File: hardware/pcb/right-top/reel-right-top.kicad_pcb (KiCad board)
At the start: 2 copper layers, 143 x 86.6 mm, 24 parts, among them SW1 choc_plate, SW10 choc_plate, SW11 choc_plate, SW12 choc_plate, SW13 choc_plate, SW14 choc_plate, SW15 choc_plate, SW16 choc_plate, SW17 choc_plate, SW18 choc_plate, SW19 choc_plate, SW2 choc_plate, SW3 choc_plate, SW4 choc_plate, SW5 choc_plate, SW6 choc_plate, SW7 choc_plate, SW8 choc_plate, SW9 choc_plate

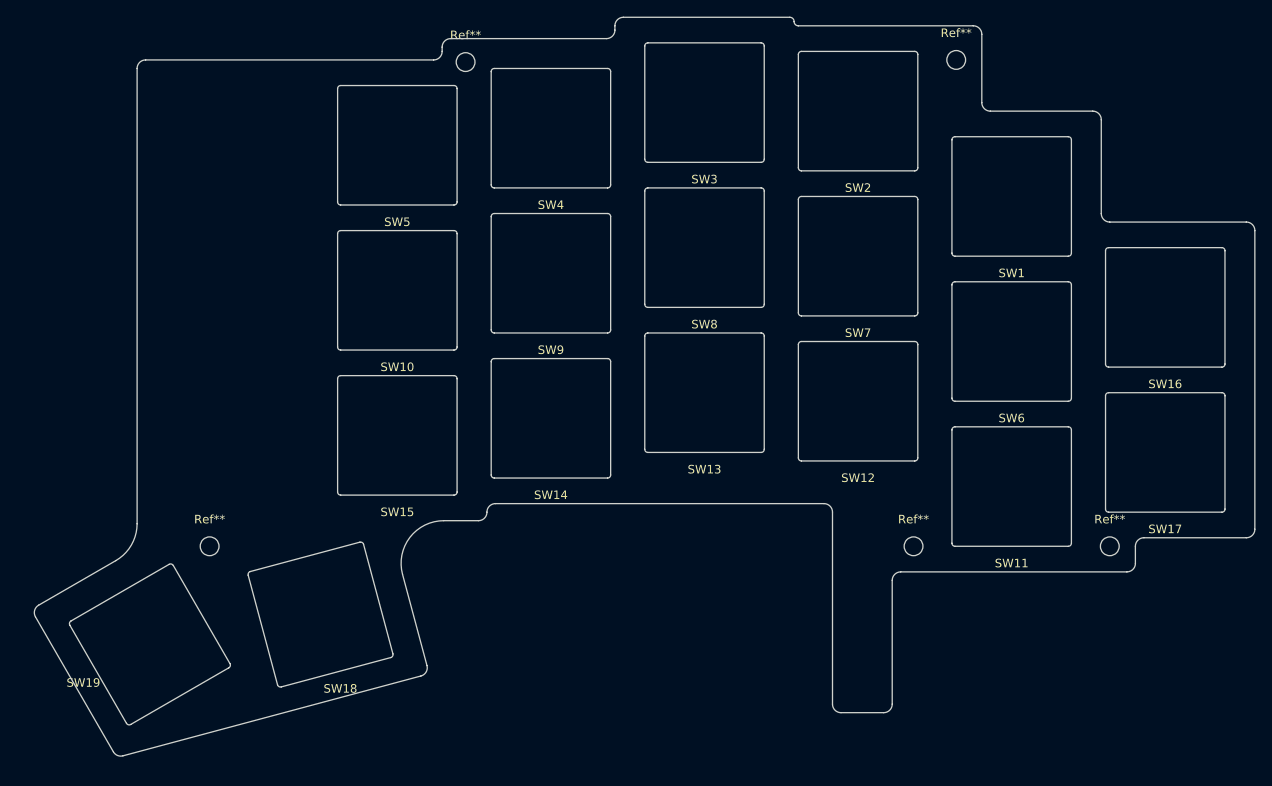
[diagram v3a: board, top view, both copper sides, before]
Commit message: Update right PCB and derived variants
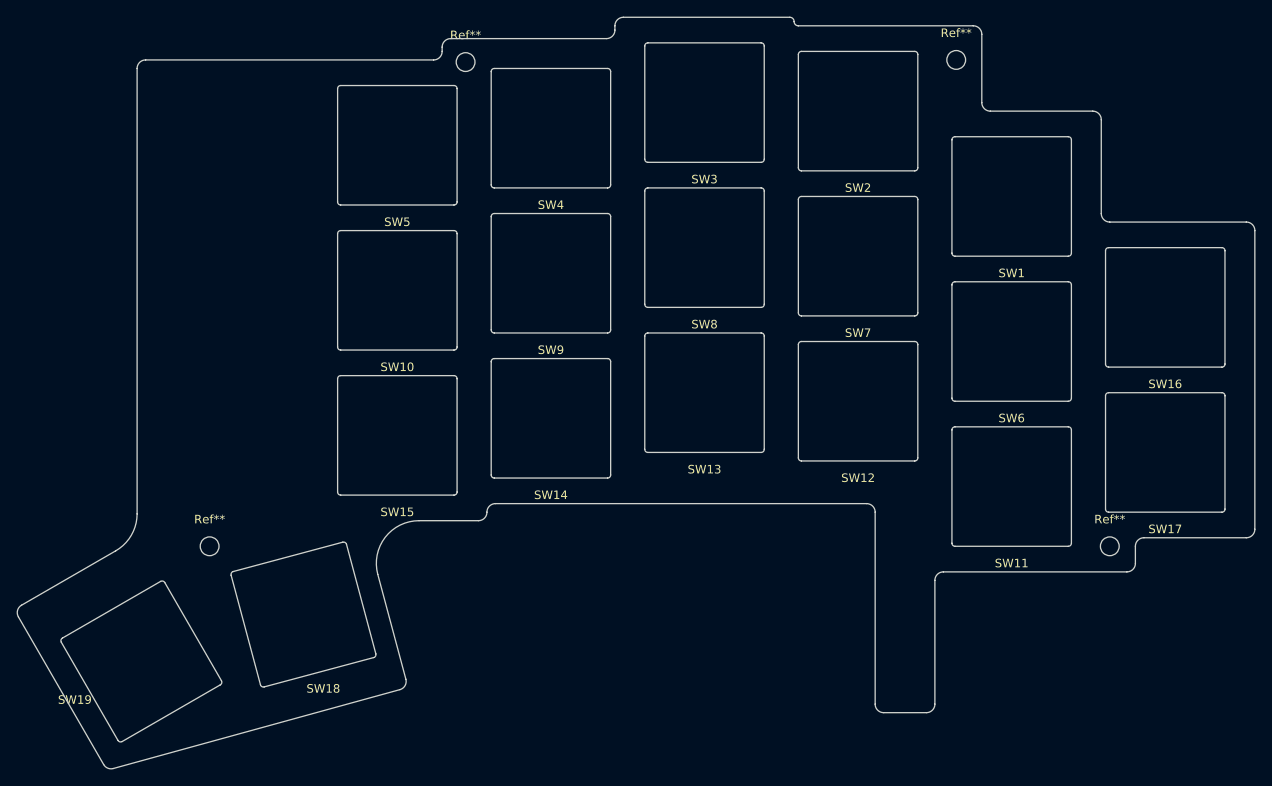
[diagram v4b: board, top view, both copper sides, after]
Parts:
- removed the Ref** at (140.5, 107.5)
- moved SW19 2.24 mm to (50.0, 121.0)
- moved SW18 2.00 mm to (69.0, 115.5)
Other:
- board size 143 x 86.6 mm -> 145 x 88.1 mm
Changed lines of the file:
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@@
 	)
 	(footprint "reel:choc_plate"
-		(generator_version "9.0")
 		(layer "F.Cu")
 		(at 116 72.5 180)
@@
 		)
 	)
-	(footprint "MountingHole:MountingHole_2.2mm_M2"
-		(layer "F.Cu")
-		(at 140.5 107.5)
-		(descr "Mounting Hole 2.2mm, M2, no annular, generated by kicad-footprint-generator mountinghole.py")
-		(tags "mountinghole M2")
-		(property "Reference" "Ref**"
-			(at 0 -3.15 0)
-			(layer "F.SilkS")
-			(effects
-				(font
-					(size 1 1)
-					(thickness 0.15)
-				)
-			)
-		)
-		(property "Value" "MountingHole_2.2mm_M2"
-			(at 0 3.15 0)
-			(layer "F.Fab")
-			(effects
-				(font
-					(size 1 1)
-					(thickness 0.15)
-				)
-			)
-		)
-		(property "KiLib_Generator" "mounting_hardware/mounting_hole"
-			(at 0 0 0)
-			(layer "F.SilkS")
-			(hide yes)
-			(effects
-				(font
-					(size 1 1)
-					(thickness 0.15)
-				)
-			)
-		)
-		(attr exclude_from_pos_files exclude_from_bom)
-		(duplicate_pad_numbers_are_jumpers no)
-		(fp_circle
-			(center 0 0)
-			(end 2.2 0)
-			(stroke
-				(width 0.15)
-				(type solid)
-			)
-			(fill no)
-			(layer "Cmts.User")
-		)
-		(fp_circle
-			(center 0 0)
-			(end 2.45 0)
-			(stroke
-				(width 0.05)
-				(type solid)
-			)
-			(fill no)
-			(layer "F.CrtYd")
-		)
-		(fp_text user "${REFERENCE}"
-			(at 0 0 0)
-			(layer "F.Fab")
-			(effects
-				(font
-					(size 1 1)
-					(thickness 0.15)
-				)
-			)
-		)
-		(pad "" np_thru_hole circle
-			(at 0 0)
-			(size 2.2 2.2)
-			(drill 2.2)
-			(layers "*.Cu" "*.Mask")
-		)
-		(embedded_fonts no)
-	)
 	(footprint "reel:choc_plate"
-		(generator_version "9.0")
 		(layer "F.Cu")
 		(at 152 100.5 180)
@@
 	)
 	(footprint "reel:choc_plate"
-		(generator_version "9.0")
 		(layer "F.Cu")
 		(at 134 90.5 180)
@@
 	)
 	(footprint "reel:choc_plate"
-		(generator_version "9.0")
 		(layer "F.Cu")
 		(at 170 96.5 180)
@@
 	)
 	(footprint "reel:choc_plate"
-		(generator_version "9.0")
 		(layer "F.Cu")
 		(at 80 60.5 180)
@@
 	)
 	(footprint "reel:choc_plate"
-		(generator_version "9.0")
 		(layer "F.Cu")
 		(at 152 66.5 180)
@@
 	)
 	(footprint "reel:choc_plate"
-		(generator_version "9.0")
 		(layer "F.Cu")
 		(at 98 75.5 180)
@@
 	)
 	(footprint "reel:choc_plate"
-		(generator_version "9.0")
 		(layer "F.Cu")
 		(at 134 56.5 180)
@@
 	)
 	(footprint "reel:choc_plate"
-		(generator_version "9.0")
 		(layer "F.Cu")
 		(at 170 79.5 180)
@@
 	)
 	(footprint "reel:choc_plate"
-		(generator_version "9.0")
 		(layer "F.Cu")
 		(at 152 83.5 180)
@@
 	)
 	(footprint "reel:choc_plate"
-		(generator_version "9.0")
 		(layer "F.Cu")
 		(at 116 55.5 180)
@@
 	)
 	(footprint "reel:choc_plate"
-		(generator_version "9.0")
 		(layer "F.Cu")
 		(at 98 92.5 180)
@@
 	)
 	(footprint "reel:choc_plate"
-		(generator_version "9.0")
 		(layer "F.Cu")
 		(at 80 77.5 180)
@@
 	)
 	(footprint "reel:choc_plate"
-		(generator_version "9.0")
 		(layer "F.Cu")
-		(at 71 115.5 -165)
+		(at 69 115.5 -165)
 		(descr "Kailh Choc V1V2 CPG1350/CPG1353 hotswap")
 		(property "Reference" "SW18"
@@
 	)
 	(footprint "reel:choc_plate"
-		(generator_version "9.0")
 		(layer "F.Cu")
 		(at 98 58.5 180)
@@
 	)
 	(footprint "reel:choc_plate"
-		(generator_version "9.0")
 		(layer "F.Cu")
 		(at 116 89.5 180)
@@
 	)
 	(footprint "reel:choc_plate"
-		(generator_version "9.0")
 		(layer "F.Cu")
-		(at 51 119 120)
+		(at 50 121 120)
 		(descr "Kailh Choc V1V2 CPG1350/CPG1353 hotswap")
 		(property "Reference" "SW19"
@@
 	)
 	(footprint "reel:choc_plate"
-		(generator_version "9.0")
 		(layer "F.Cu")
 		(at 134 73.5 180)
@@
 	)
 	(footprint "reel:choc_plate"
-		(generator_version "9.0")
 		(layer "F.Cu")
 		(at 80 94.5 180)
@@
 	)
 	(gr_arc
-		(start 37.589746 115.772758)
-		(mid 37.489877 115.013958)
-		(end 37.955771 114.406733)
+		(start 35.589762 115.772786)
+		(mid 35.489859 115.013966)
+		(end 35.955785 114.406758)
 		(stroke
 			(width 0.05)
@@
 	)
 	(gr_line
-		(start 37.589746 115.772758)
-		(end 46.722209 131.590648)
+		(start 35.589762 115.772786)
+		(end 45.582283 133.0802)
 		(stroke
 			(width 0.05)
@@
 		(layer "Edge.Cuts")
 	)
+	(gr_arc
+		(start 46.713675 133.544345)
+		(mid 46.068759 133.505375)
+		(end 45.582283 133.0802)
+		(stroke
+			(width 0.05)
+			(type default)
+		)
+		(layer "Edge.Cuts")
+	)
 	(gr_line
-		(start 37.955771 114.406733)
-		(end 47 109.185045)
+		(start 46.713675 133.544345)
+		(end 80.29895 124.300482)
 		(stroke
 			(width 0.05)
@@
 		(layer "Edge.Cuts")
 	)
-	(gr_arc
-		(start 47.847054 132.056574)
-		(mid 47.205532 132.014546)
-		(end 46.722209 131.590648)
+	(gr_line
+		(start 47 108.030377)
+		(end 35.955785 114.406758)
 		(stroke
 			(width 0.05)
-			(type default)
+			(type solid)
 		)
 		(layer "Edge.Cuts")
@@
 	(gr_line
 		(start 49.5 51.5)
-		(end 49.5 104.854918)
+		(end 49.5 103.70025)
 		(stroke
 			(width 0.05)
@@
 	)
 	(gr_arc
-		(start 49.5 104.854918)
-		(mid 48.83012 107.354912)
-		(end 47 109.185045)
+		(start 49.5 103.70025)
+		(mid 48.830108 106.200232)
+		(end 47 108.030377)
 		(stroke
 			(width 0.05)
@@
 	)
 	(gr_arc
-		(start 80.609457 110.794095)
-		(mid 81.47232 106.456193)
-		(end 85.439086 104.5)
+		(start 77.708196 110.794087)
+		(mid 78.571063 106.45619)
+		(end 82.537827 104.5)
 		(stroke
 			(width 0.05)
@@
 	)
 	(gr_line
-		(start 82.764485 122.700476)
-		(end 47.847054 132.056574)
+		(start 80.999508 123.077517)
+		(end 77.708196 110.794087)
 		(stroke
 			(width 0.05)
@@
 		(layer "Edge.Cuts")
 	)
-	(gr_line
-		(start 83.471592 121.475731)
-		(end 80.609457 110.794095)
+	(gr_arc
+		(start 80.999508 123.077517)
+		(mid 80.901298 123.833393)
+		(end 80.29895 124.300482)
 		(stroke
 			(width 0.05)
-			(type solid)
+			(type default)
 		)
 		(layer "Edge.Cuts")
 	)
-	(gr_arc
-		(start 83.471592 121.475731)
-		(mid 83.371665 122.234514)
-		(end 82.764485 122.700476)
+	(gr_line
+		(start 82.537827 104.5)
+		(end 89.5 104.5)
 		(stroke
 			(width 0.05)
@@
 		(layer "Edge.Cuts")
 	)
-	(gr_line
-		(start 89.5 104.5)
-		(end 85.439086 104.5)
-		(stroke
-			(width 0.05)
-			(type default)
-		)
-		(layer "Edge.Cuts")
-	)
 	(gr_arc
 		(start 90.5 103.5)
@@
 	(gr_line
 		(start 91.5 102.5)
-		(end 130 102.5)
+		(end 135 102.5)
 		(stroke
 			(width 0.05)
@@
 	)
 	(gr_arc
-		(start 130 102.5)
-		(mid 130.707107 102.792893)
-		(end 131 103.5)
+		(start 135 102.5)
+		(mid 135.707107 102.792893)
+		(end 136 103.5)
 		(stroke
 			(width 0.05)
@@
 	)
 	(gr_line
-		(start 131 126)
-		(end 131 103.5)
+		(start 136 126)
+		(end 136 103.5)
 		(stroke
 			(width 0.05)
@@
 	)
 	(gr_arc
-		(start 132 127)
-		(mid 131.292893 126.707107)
-		(end 131 126)
+		(start 137 127)
+		(mid 136.292893 126.707107)
+		(end 136 126)
 		(stroke
 			(width 0.05)
@@
 	)
 	(gr_line
-		(start 137 127)
-		(end 132 127)
+		(start 142 127)
+		(end 137 127)
 		(stroke
 			(width 0.05)
@@
 	)
 	(gr_line
-		(start 138 111.5)
-		(end 138 126)
+		(start 143 111.5)
+		(end 143 126)
 		(stroke
 			(width 0.05)
@@
 	)
 	(gr_arc
-		(start 138 111.5)
-		(mid 138.292893 110.792893)
-		(end 139 110.5)
+		(start 143 111.5)
+		(mid 143.292893 110.792893)
+		(end 144 110.5)
 		(stroke
 			(width 0.05)
@@
 	)
 	(gr_arc
-		(start 138 126)
-		(mid 137.707107 126.707107)
-		(end 137 127)
+		(start 143 126)
+		(mid 142.707107 126.707107)
+		(end 142 127)
 		(stroke
 			(width 0.05)
@@
 	(gr_line
 		(start 165.5 110.5)
-		(end 139 110.5)
+		(end 144 110.5)
 		(stroke
 			(width 0.05)
